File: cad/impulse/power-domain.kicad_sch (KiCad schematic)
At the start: 21 parts, among them Q2 Q_PMOS_DGS, U1 MT2492, U2 MT2492

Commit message: Calculated smps values and modified .gitignore.
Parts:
- added JP101: Jumper_2_Open, Jumper:SolderJumper-2_P1.3mm_Open_TrianglePad1.0x1.5mm, symbol Jumper:Jumper_2_Open
- C1, C4: value C_Small -> 22n
- C10, C3, C6, C7, C8, C9: value C_Small -> 22u
- C2, C5: value C_Small -> 22p
- L1: value L_Small -> 22u
- L2: value L_Small -> 10u
- R1, R3: value R_Small -> 100k
- R2: value R_Small -> 22k1
- R4: value R_Small -> 13.3
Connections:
- net vinp: now also C10.1, C3.1, U1.4 (EN), U1.5 (IN), U2.4 (EN), U2.5 (IN)
- net +3V3: now reaches C2.1, C8.1, C9.1, L1.2, R1.1
- net at C5.1, C6.1, C7.1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: now also JP101.1 (A)
- new net +5V: JP101.2 (B)
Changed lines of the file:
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@@
 (kicad_sch (version 20230121) (generator eeschema)
   (paper "A4")
+  (junction (at 251.46 29.21) (diameter 0) (color 0 0 0 0)
+  )
+  (junction (at 152.4 29.21) (diameter 0) (color 0 0 0 0)
+  )
   (junction (at 236.22 29.21) (diameter 0) (color 0 0 0 0)
   )
@@
   )
   (wire (pts (xy 195.58 29.21) (xy 201.93 29.21))
+    (stroke (width 0) (type default))
+  )
+  (wire (pts (xy 152.4 29.21) (xy 161.29 29.21))
     (stroke (width 0) (type default))
   )
@@
     (stroke (width 0) (type default))
   )
+  (wire (pts (xy 251.46 29.21) (xy 254 29.21))
+    (stroke (width 0) (type default))
+  )
   (polyline (pts (xy 12.7 57.15) (xy 74.93 57.15))
     (stroke (width 0) (type dash))
@@
     (effects (font (size 1.27 1.27) (thickness 0.254) bold) (justify left bottom))
   )
+  (label "vinp" (at 195.58 29.21 180) (fields_autoplaced)
+    (effects (font (size 1.27 1.27)) (justify right bottom))
+  )
+  (label "vinp" (at 96.52 29.21 180) (fields_autoplaced)
+    (effects (font (size 1.27 1.27)) (justify right bottom))
+  )
   (label "vinp" (at 63.5 30.48 0) (fields_autoplaced)
     (effects (font (size 1.27 1.27)) (justify left bottom))
@@
     )
   )
+  (symbol (lib_id "power:+3V3") (at 161.29 29.21 0) (unit 1)
+    (in_bom yes) (on_board yes) (dnp no) (fields_autoplaced)
+    (property "Reference" "#PWR011" (at 161.29 33.02 0)
+      (effects (font (size 1.27 1.27)) hide)
+    )
+    (property "Value" "+3V3" (at 161.29 25.4 0)
+      (effects (font (size 1.27 1.27)))
+    )
+    (property "Footprint" "" (at 161.29 29.21 0)
+      (effects (font (size 1.27 1.27)) hide)
+    )
+    (property "Datasheet" "" (at 161.29 29.21 0)
+      (effects (font (size 1.27 1.27)) hide)
+    )
+    (pin "1")
+    (instances
+      (project "impulse"
+        (path "/eb4cfece-5fcb-437a-ac58-337ab6512039/8b8b63e5-7f69-4185-825a-2602e0d2cd2e"
+          (reference "#PWR011") (unit 1)
+        )
+      )
+    )
+  )
   (symbol (lib_id "Device:R_Small") (at 127 36.83 0) (unit 1)
     (in_bom yes) (on_board yes) (dnp no)
@@
       (effects (font (size 1.27 1.27)) (justify left))
     )
-    (property "Value" "R_Small" (at 128.27 38.1 0)
+    (property "Value" "22k1" (at 128.27 38.1 0)
       (effects (font (size 1.27 1.27)) (justify left))
     )
@@
   )
   (symbol (lib_id "Device:L_Small") (at 124.46 29.21 90) (unit 1)
-    (in_bom yes) (on_board yes) (dnp no) (fields_autoplaced)
-    (property "Reference" "L1" (at 124.46 25.4 90)
-      (effects (font (size 1.27 1.27)))
-    )
-    (property "Value" "L_Small" (at 124.46 27.94 90)
+    (in_bom yes) (on_board yes) (dnp no)
+    (property "Reference" "L1" (at 124.46 24.13 90)
+      (effects (font (size 1.27 1.27)))
+    )
+    (property "Value" "22u" (at 124.46 26.67 90)
       (effects (font (size 1.27 1.27)))
     )
@@
     )
   )
+  (symbol (lib_id "power:+5V") (at 264.16 29.21 0) (unit 1)
+    (in_bom yes) (on_board yes) (dnp no) (fields_autoplaced)
+    (property "Reference" "#PWR010" (at 264.16 33.02 0)
+      (effects (font (size 1.27 1.27)) hide)
+    )
+    (property "Value" "+5V" (at 264.16 25.4 0)
+      (effects (font (size 1.27 1.27)))
+    )
+    (property "Footprint" "" (at 264.16 29.21 0)
+      (effects (font (size 1.27 1.27)) hide)
+    )
+    (property "Datasheet" "" (at 264.16 29.21 0)
+      (effects (font (size 1.27 1.27)) hide)
+    )
+    (pin "1")
+    (instances
+      (project "impulse"
+        (path "/eb4cfece-5fcb-437a-ac58-337ab6512039/8b8b63e5-7f69-4185-825a-2602e0d2cd2e"
+          (reference "#PWR010") (unit 1)
+        )
+      )
+    )
+  )
   (symbol (lib_id "power:GND") (at 96.52 34.29 0) (unit 1)
     (in_bom yes) (on_board yes) (dnp no) (fields_autoplaced)
@@
   (symbol (lib_id "Device:C_Small") (at 96.52 31.75 0) (unit 1)
     (in_bom yes) (on_board yes) (dnp no)
-    (property "Reference" "C10" (at 92.71 24.13 0)
-      (effects (font (size 1.27 1.27)))
-    )
-    (property "Value" "C_Small" (at 95.25 26.67 0)
+    (property "Reference" "C10" (at 95.25 22.86 0)
+      (effects (font (size 1.27 1.27)))
+    )
+    (property "Value" "22u" (at 95.25 25.4 0)
       (effects (font (size 1.27 1.27)))
     )
@@
   (symbol (lib_id "Device:C_Small") (at 247.65 31.75 0) (unit 1)
     (in_bom yes) (on_board yes) (dnp no)
-    (property "Reference" "C6" (at 243.84 24.13 0)
-      (effects (font (size 1.27 1.27)))
-    )
-    (property "Value" "C_Small" (at 246.38 26.67 0)
+    (property "Reference" "C6" (at 247.65 24.13 0)
+      (effects (font (size 1.27 1.27)))
+    )
+    (property "Value" "22u" (at 247.65 26.67 0)
       (effects (font (size 1.27 1.27)))
     )
@@
   (symbol (lib_id "Device:C_Small") (at 195.58 31.75 0) (unit 1)
     (in_bom yes) (on_board yes) (dnp no)
-    (property "Reference" "C3" (at 191.77 24.13 0)
-      (effects (font (size 1.27 1.27)))
-    )
-    (property "Value" "C_Small" (at 194.31 26.67 0)
+    (property "Reference" "C3" (at 193.04 22.86 0)
+      (effects (font (size 1.27 1.27)))
+    )
+    (property "Value" "22u" (at 193.04 25.4 0)
       (effects (font (size 1.27 1.27)))
     )
@@
   (symbol (lib_id "Device:C_Small") (at 137.16 31.75 0) (unit 1)
     (in_bom yes) (on_board yes) (dnp no)
-    (property "Reference" "C2" (at 135.89 24.13 0)
-      (effects (font (size 1.27 1.27)))
-    )
-    (property "Value" "C_Small" (at 138.43 26.67 0)
+    (property "Reference" "C2" (at 137.16 24.13 0)
+      (effects (font (size 1.27 1.27)))
+    )
+    (property "Value" "22p" (at 137.16 26.67 0)
       (effects (font (size 1.27 1.27)))
     )
@@
       (effects (font (size 1.27 1.27)) (justify left))
     )
-    (property "Value" "R_Small" (at 128.27 33.02 0)
+    (property "Value" "100k" (at 128.27 33.02 0)
       (effects (font (size 1.27 1.27)) (justify left))
     )
@@
   )
   (symbol (lib_id "Device:L_Small") (at 223.52 29.21 90) (unit 1)
-    (in_bom yes) (on_board yes) (dnp no) (fields_autoplaced)
-    (property "Reference" "L2" (at 223.52 25.4 90)
-      (effects (font (size 1.27 1.27)))
-    )
-    (property "Value" "L_Small" (at 223.52 27.94 90)
+    (in_bom yes) (on_board yes) (dnp no)
+    (property "Reference" "L2" (at 223.52 24.13 90)
+      (effects (font (size 1.27 1.27)))
+    )
+    (property "Value" "10u" (at 223.52 26.67 90)
       (effects (font (size 1.27 1.27)))
     )
@@
   (symbol (lib_id "Device:C_Small") (at 148.59 31.75 0) (unit 1)
     (in_bom yes) (on_board yes) (dnp no)
-    (property "Reference" "C8" (at 144.78 24.13 0)
-      (effects (font (size 1.27 1.27)))
-    )
-    (property "Value" "C_Small" (at 147.32 26.67 0)
+    (property "Reference" "C8" (at 147.32 24.13 0)
+      (effects (font (size 1.27 1.27)))
+    )
+    (property "Value" "22u" (at 147.32 26.67 0)
       (effects (font (size 1.27 1.27)))
     )
@@
       (effects (font (size 1.27 1.27)))
     )
-    (property "Value" "C_Small" (at 154.94 26.67 0)
+    (property "Value" "22u" (at 152.4 26.67 0)
       (effects (font (size 1.27 1.27)))
     )
@@
       (effects (font (size 1.27 1.27)))
     )
-    (property "Value" "C_Small" (at 121.92 21.59 90)
+    (property "Value" "22n" (at 119.38 21.59 90)
       (effects (font (size 1.27 1.27)))
     )
@@
     )
   )
+  (symbol (lib_id "Jumper:Jumper_2_Open") (at 259.08 29.21 0) (unit 1)
+    (in_bom yes) (on_board yes) (dnp no)
+    (property "Reference" "JP101" (at 261.62 31.75 0)
+      (effects (font (size 1.27 1.27)))
+    )
+    (property "Value" "Jumper_2_Open" (at 261.62 34.29 0)
+      (effects (font (size 1.27 1.27)))
+    )
+    (property "Footprint" "Jumper:SolderJumper-2_P1.3mm_Open_TrianglePad1.0x1.5mm" (at 259.08 29.21 0)
+      (effects (font (size 1.27 1.27)) hide)
+    )
+    (property "Datasheet" "~" (at 259.08 29.21 0)
+      (effects (font (size 1.27 1.27)) hide)
+    )
+    (pin "1")
+    (pin "2")
+    (instances
+      (project "valentine"
+        (path "/1e598ca5-0882-4bb6-9d64-e7e7f53f92db"
+          (reference "JP101") (unit 1)
+        )
+      )
+      (project "impulse"
+        (path "/eb4cfece-5fcb-437a-ac58-337ab6512039/8b8b63e5-7f69-4185-825a-2602e0d2cd2e"
+          (reference "JP2") (unit 1)
+        )
+      )
+    )
+  )
   (symbol (lib_id "Device:C_Small") (at 215.9 24.13 90) (unit 1)
     (in_bom yes) (on_board yes) (dnp no)
@@
       (effects (font (size 1.27 1.27)))
     )
-    (property "Value" "C_Small" (at 220.98 21.59 90)
+    (property "Value" "22n" (at 218.44 21.59 90)
       (effects (font (size 1.27 1.27)))
     )
@@
       (effects (font (size 1.27 1.27)))
     )
-    (property "Value" "C_Small" (at 254 26.67 0)
+    (property "Value" "22u" (at 251.46 26.67 0)
       (effects (font (size 1.27 1.27)))
     )
@@
       (effects (font (size 1.27 1.27)) (justify left))
     )
-    (property "Value" "R_Small" (at 227.33 38.1 0)
+    (property "Value" "13.3" (at 227.33 38.1 0)
       (effects (font (size 1.27 1.27)) (justify left))
     )
@@
       (effects (font (size 1.27 1.27)) (justify left))
     )
-    (property "Value" "R_Small" (at 227.33 33.02 0)
+    (property "Value" "100k" (at 227.33 33.02 0)
       (effects (font (size 1.27 1.27)) (justify left))
     )
@@
       (effects (font (size 1.27 1.27)))
     )
-    (property "Value" "C_Small" (at 237.49 26.67 0)
-      (effects (font (size 1.27 1.27)))
-    )
+    (property "Value" "22p" (at 234.95 26.67 0)
+      (effects (font (size 1.27 1.27)))
+    )

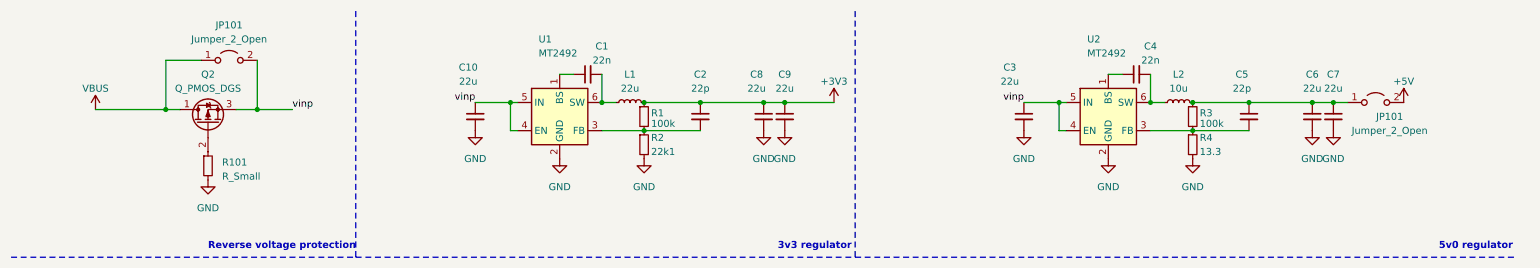
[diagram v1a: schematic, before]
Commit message: Added IMU, button and led. Moved things around.
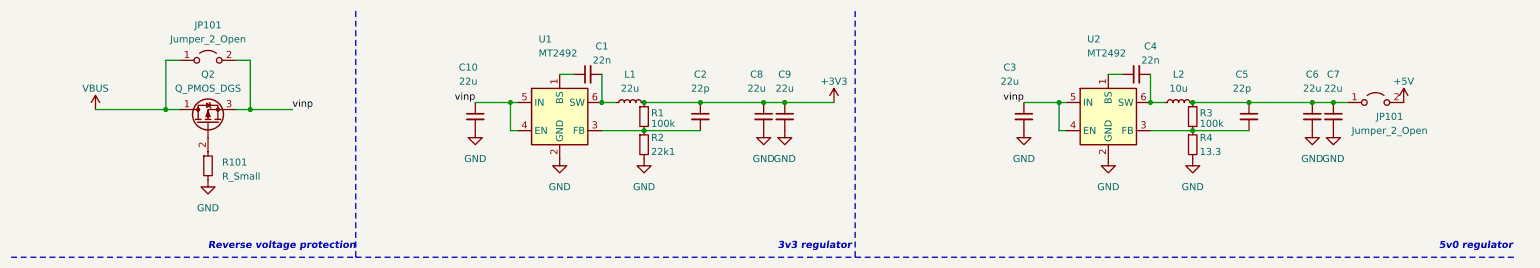
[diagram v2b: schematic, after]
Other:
- moved on the sheet: JP101
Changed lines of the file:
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@@
   (junction (at 236.22 29.21) (diameter 0) (color 0 0 0 0)
   )
+  (junction (at 55.88 30.48) (diameter 0) (color 0 0 0 0)
+  )
   (junction (at 119.38 29.21) (diameter 0) (color 0 0 0 0)
   )
@@
   (junction (at 226.06 29.21) (diameter 0) (color 0 0 0 0)
   )
-  (junction (at 57.15 30.48) (diameter 0) (color 0 0 0 0)
-  )
   (junction (at 40.64 30.48) (diameter 0) (color 0 0 0 0)
   )
@@
   (junction (at 137.16 29.21) (diameter 0) (color 0 0 0 0)
   )
+  (wire (pts (xy 55.88 30.48) (xy 53.34 30.48))
+    (stroke (width 0) (type default))
+  )
   (wire (pts (xy 236.22 29.21) (xy 247.65 29.21))
-    (stroke (width 0) (type default))
-  )
-  (wire (pts (xy 53.34 30.48) (xy 57.15 30.48))
     (stroke (width 0) (type default))
   )
@@
     (stroke (width 0) (type default))
   )
-  (wire (pts (xy 57.15 30.48) (xy 63.5 30.48))
-    (stroke (width 0) (type default))
-  )
   (wire (pts (xy 40.64 30.48) (xy 43.18 30.48))
     (stroke (width 0) (type default))
   )
   (wire (pts (xy 218.44 29.21) (xy 220.98 29.21))
+    (stroke (width 0) (type default))
+  )
+  (wire (pts (xy 55.88 30.48) (xy 63.5 30.48))
     (stroke (width 0) (type default))
   )
@@
     (stroke (width 0) (type default))
   )
-  (wire (pts (xy 57.15 21.59) (xy 57.15 30.48))
+  (wire (pts (xy 55.88 21.59) (xy 55.88 30.48))
     (stroke (width 0) (type default))
   )
@@
     (stroke (width 0) (type dash))
   )
-  (wire (pts (xy 46.99 21.59) (xy 40.64 21.59))
+  (wire (pts (xy 43.18 21.59) (xy 40.64 21.59))
+    (stroke (width 0) (type default))
+  )
+  (wire (pts (xy 55.88 21.59) (xy 53.34 21.59))
     (stroke (width 0) (type default))
   )
@@
   )
   (text "5v0 regulator" (at 270.51 55.88 0)
-    (effects (font (size 1.27 1.27) (thickness 0.254) bold) (justify left bottom))
+    (effects (font (size 1.27 1.27) (thickness 0.254) bold italic) (justify left bottom))
   )
   (text "3v3 regulator" (at 151.13 55.88 0)
-    (effects (font (size 1.27 1.27) (thickness 0.254) bold) (justify left bottom))
+    (effects (font (size 1.27 1.27) (thickness 0.254) bold italic) (justify left bottom))
   )
   (text "Reverse voltage protection" (at 48.26 55.88 0)
-    (effects (font (size 1.27 1.27) (thickness 0.254) bold) (justify left bottom))
+    (effects (font (size 1.27 1.27) (thickness 0.254) bold italic) (justify left bottom))
   )
   (label "vinp" (at 195.58 29.21 180) (fields_autoplaced)
@@
     )
   )
-  (symbol (lib_id "Jumper:Jumper_2_Open") (at 52.07 21.59 0) (unit 1)
-    (in_bom yes) (on_board yes) (dnp no) (fields_autoplaced)
-    (property "Reference" "JP101" (at 52.07 15.24 0)
-      (effects (font (size 1.27 1.27)))
-    )
-    (property "Value" "Jumper_2_Open" (at 52.07 17.78 0)
-      (effects (font (size 1.27 1.27)))
-    )
-    (property "Footprint" "Jumper:SolderJumper-2_P1.3mm_Open_TrianglePad1.0x1.5mm" (at 52.07 21.59 0)
-      (effects (font (size 1.27 1.27)) hide)
-    )
-    (property "Datasheet" "~" (at 52.07 21.59 0)
-      (effects (font (size 1.27 1.27)) hide)
-    )
+  (symbol (lib_id "Jumper:Jumper_2_Open") (at 48.26 21.59 0) (unit 1)
+    (in_bom yes) (on_board yes) (dnp no) (fields_autoplaced)
+    (property "Reference" "JP101" (at 48.26 15.24 0)
+      (effects (font (size 1.27 1.27)))
+    )
+    (property "Value" "Jumper_2_Open" (at 48.26 17.78 0)
+      (effects (font (size 1.27 1.27)))
+    )
+    (property "Footprint" "Jumper:SolderJumper-2_P1.3mm_Open_TrianglePad1.0x1.5mm" (at 48.26 21.59 0)
+      (effects (font (size 1.27 1.27)) hide)
+    )
+    (property "Datasheet" "~" (at 48.26 21.59 0)
+      (effects (font (size 1.27 1.27)) hide)
+    )

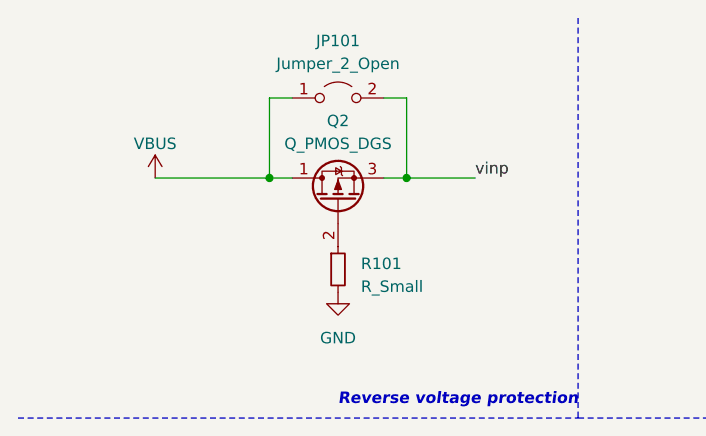
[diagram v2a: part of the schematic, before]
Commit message: Added USB connector.
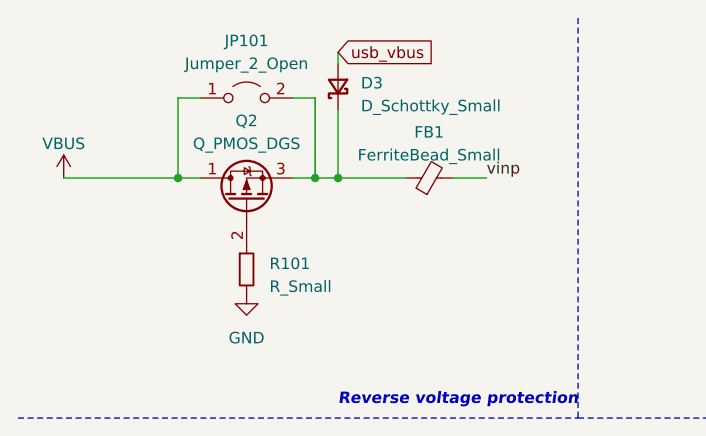
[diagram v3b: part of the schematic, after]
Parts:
- added D3: D_Schottky_Small, symbol Device:D_Schottky_Small
- added FB1: FerriteBead_Small, symbol Device:FerriteBead_Small
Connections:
- net vinp: now also FB1.2; no longer JP101.2 (B), Q2.3 (S)
- new net: D3.1 (K), FB1.1, JP101.2 (B), Q2.3 (S)
- new net usb_vbus: D3.2 (A)
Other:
- moved on the sheet: JP101, Q2, R101

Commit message: Finished with LoRa.
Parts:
- renumbered C7 to C10, C4 to C2, C10 to C3, C2 to C4, C8 to C5, C9 to C6, C3 to C7, C5 to C8, C6 to C9, D3 to D1, Q2 to Q1, R3 to R2, R2 to R3

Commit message: Finnished the design.
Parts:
- removed JP101: Jumper_2_Open, Jumper:SolderJumper-2_P1.3mm_Open_TrianglePad1.0x1.5mm, symbol Jumper:Jumper_2_Open
- removed Q1: Q_PMOS_DGS, symbol Device:Q_PMOS_DGS
- added D7: MM3Z10B, symbol Device:D_Zener_Small
- added Q101: AO3415, symbol Device:Q_PMOS_GSD
- D1: value D_Schottky_Small -> DSK14W
- FB1: value FerriteBead_Small -> CBM201209U600T
- JP101: footprint Jumper:SolderJumper-2_P1.3mm_Open_TrianglePad1.0x1.5mm -> (none)
- R101: value R_Small -> 22k1; footprint Resistor_SMD:R_0603_1608Metric -> (none)
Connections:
- net VBUS: now also Q101.3 (D)
- net at D1.1 (K), FB1.1: now also D7.1 (K), Q101.2 (S)
- net at R101.1: now also D7.2 (A), Q101.1 (G)
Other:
- company: (none) -> markbel
- title: (none) -> Power

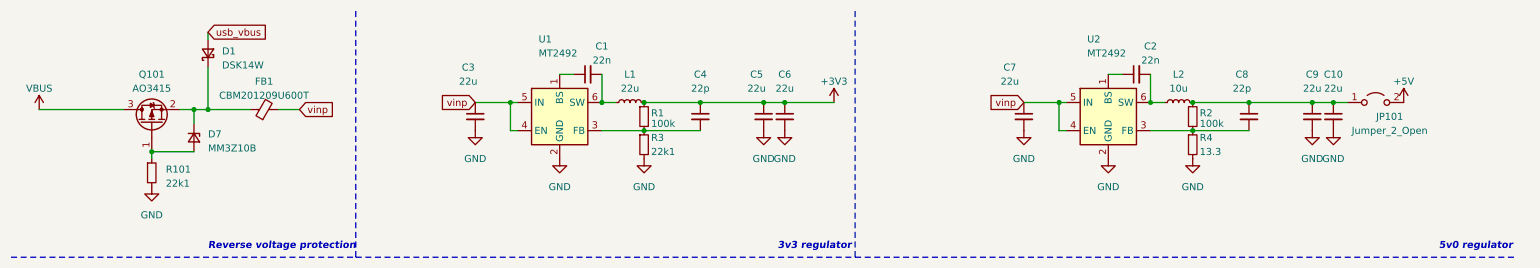
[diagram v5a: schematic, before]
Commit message: Started working on BOM, did consolidation.
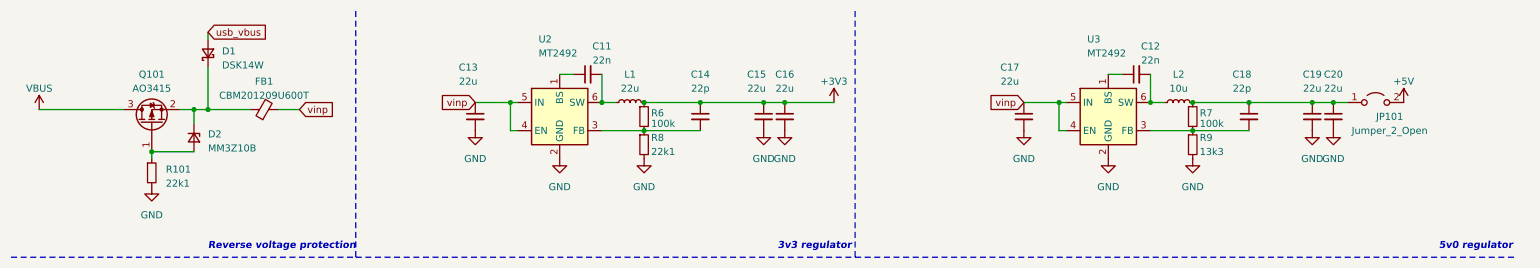
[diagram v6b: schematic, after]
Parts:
- C11: renamed from C1; lcsc (none) -> C5137627
- C12: renamed from C2; lcsc (none) -> C5137627
- C13: renamed from C3; lcsc (none) -> C2858005
- C14: renamed from C4; lcsc (none) -> C5137569
- C15: renamed from C5; lcsc (none) -> C2858005
- C16: renamed from C6; lcsc (none) -> C2858005
- C17: renamed from C7; lcsc (none) -> C2858005
- C18: renamed from C8; lcsc (none) -> C5137569
- C19: renamed from C9; lcsc (none) -> C2858005
- C20: renamed from C10; lcsc (none) -> C2858005
- D1: lcsc (none) -> C3014043
- D2: renamed from D7; lcsc (none) -> C2826565
- FB1: lcsc (none) -> C139167
- L1: lcsc (none) -> C223225
- L2: lcsc (none) -> C2921170
- Q101: lcsc (none) -> C181094
- R101: lcsc (none) -> C5356129
- R6: renamed from R1; lcsc (none) -> C3017514
- R7: renamed from R2; lcsc (none) -> C3017514
- R8: renamed from R3; lcsc (none) -> C5356129
- R9: renamed from R4; value 13.3 -> 13k3; lcsc (none) -> C3015832
- U2: renamed from U1; lcsc (none) -> C89358
- U3: renamed from U2; lcsc (none) -> C89358
